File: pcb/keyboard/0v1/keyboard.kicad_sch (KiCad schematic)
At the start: 9 parts, among them U1 113990583

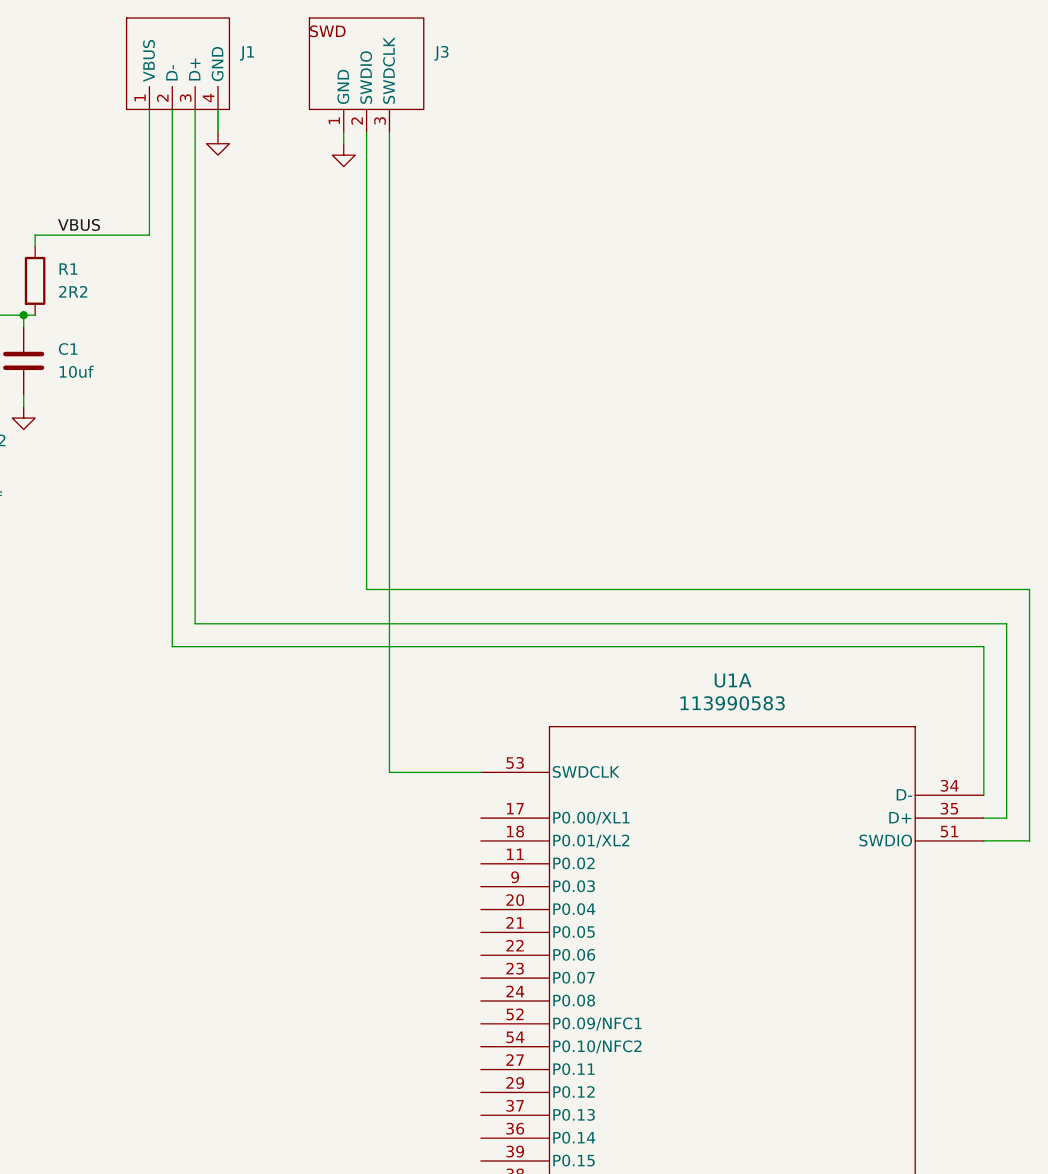
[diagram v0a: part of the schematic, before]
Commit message: MCU components complete.
Only keyboard components and layout to go.
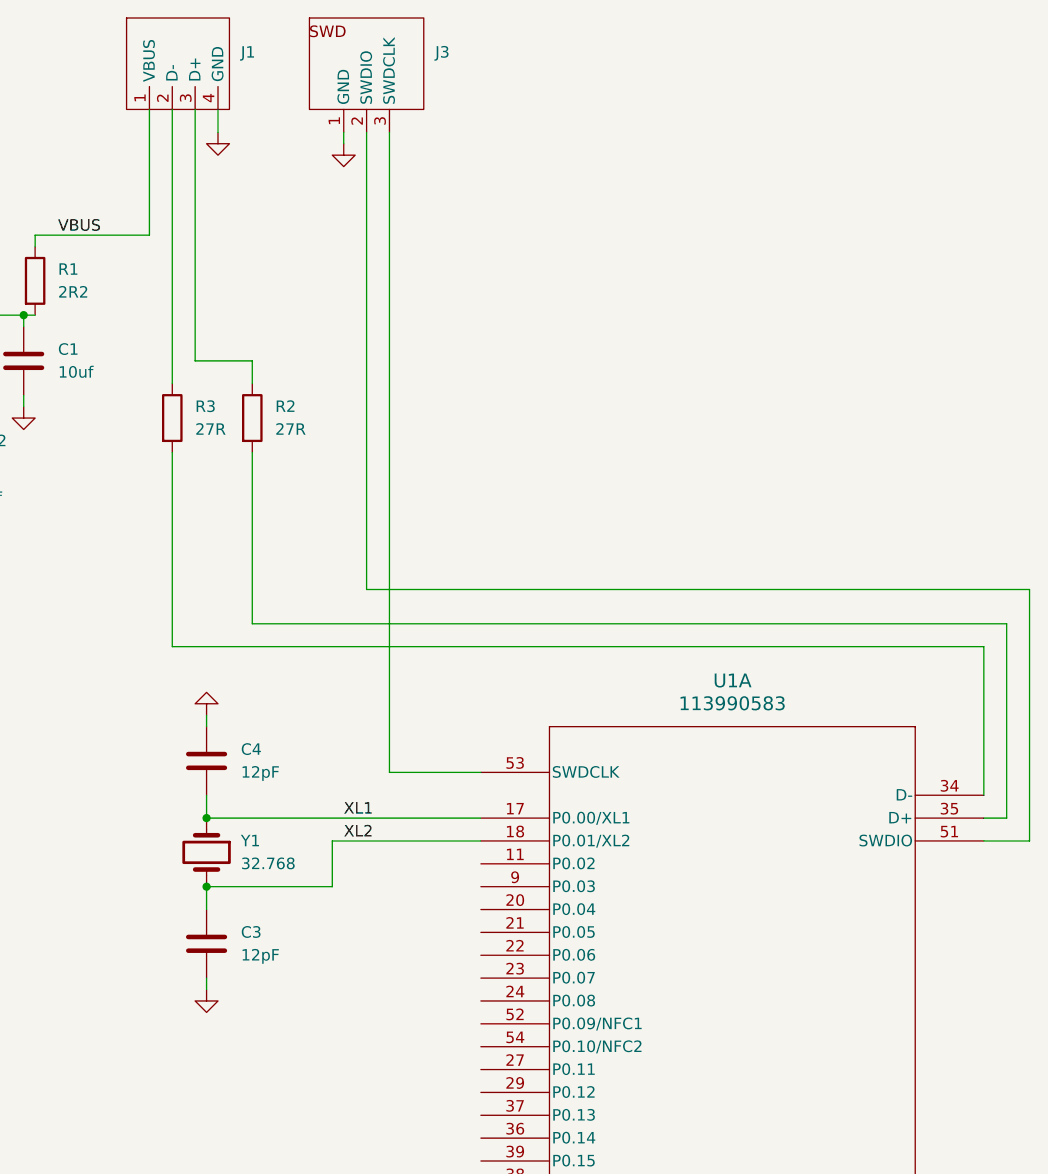
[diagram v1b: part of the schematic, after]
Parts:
- added C3, C4: 12pF, Capacitor_SMD:C_0603_1608Metric, symbol Device:C
- added R2, R3: 27R, Resistor_SMD:R_0603_1608Metric, symbol Device:R
- added Y1: 32.768, Crystal:Crystal_SMD_3215-2Pin_3.2x1.5mm, symbol Device:Crystal
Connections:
- net GND: now also C3.1, C4.2
- net at J1.2 (D-): now also R3.1; no longer U1.34 (D-)
- net at J1.3 (D+): now also R2.1; no longer U1.35 (D+)
- net XL1: now reaches U1.17 (P0.00/XL1)
- net XL1: now also C4.1, Y1.1
- net XL2: now reaches U1.18 (P0.01/XL2)
- net XL2: now also C3.2, Y1.2
- new net: R2.2, U1.35 (D+)
- new net: R3.2, U1.34 (D-)
